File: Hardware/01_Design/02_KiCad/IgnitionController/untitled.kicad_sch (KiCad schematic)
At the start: 26 parts, among them Q4 RSJ250P10, Q5 BC856, Q6 IRF9Z34NSPbF, U3 LM2575-3.3BU, U4 LM2575-5.0BU

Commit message: PMIC HW implementation
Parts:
- added C11: UCL1V101MNL1GS, Capacitor_SMD:CP_Elec_8x11.9, symbol Device:C_Polarized
- added C12: UCL1V331MNL1GS, Capacitor_SMD:CP_Elec_10x12.5, symbol Device:C_Polarized
- added D15: SS14, Diode_SMD:D_SMA, symbol Diode:SS14
- added D16: RED, LED_SMD:LED_0805_2012Metric_Pad1.15x1.40mm_HandSolder, symbol Device:LED
- added L5: L_Iron, Inductor_SMD:L_7.3x7.3_H3.5, symbol Device:L_Iron
- added R23: 470R, Resistor_SMD:R_0805_2012Metric_Pad1.20x1.40mm_HandSolder, symbol Device:R
- added U9: LM2575-5.0BU, Package_TO_SOT_SMD:TO-263-5_TabPin3, symbol Regulator_Switching:LM2575-5.0BU
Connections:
- net GND: now also C11.2, C12.2, D15.2 (A), D16.1 (K), U9.3 (GND), U9.5 (~{ON}/OFF)
- net VCC: now also C11.1, U9.1 (VIN)
- new net: D15.1 (K), L5.1, U9.2 (OUT)
- new net: D16.2 (A), R23.2
- new net VPMIC: C12.1, L5.2, R23.1, U9.4 (FB)
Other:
- note added: "VSEN VMCU and VPMIC power supply"
- note removed: "VSEN and VMCU power supply"

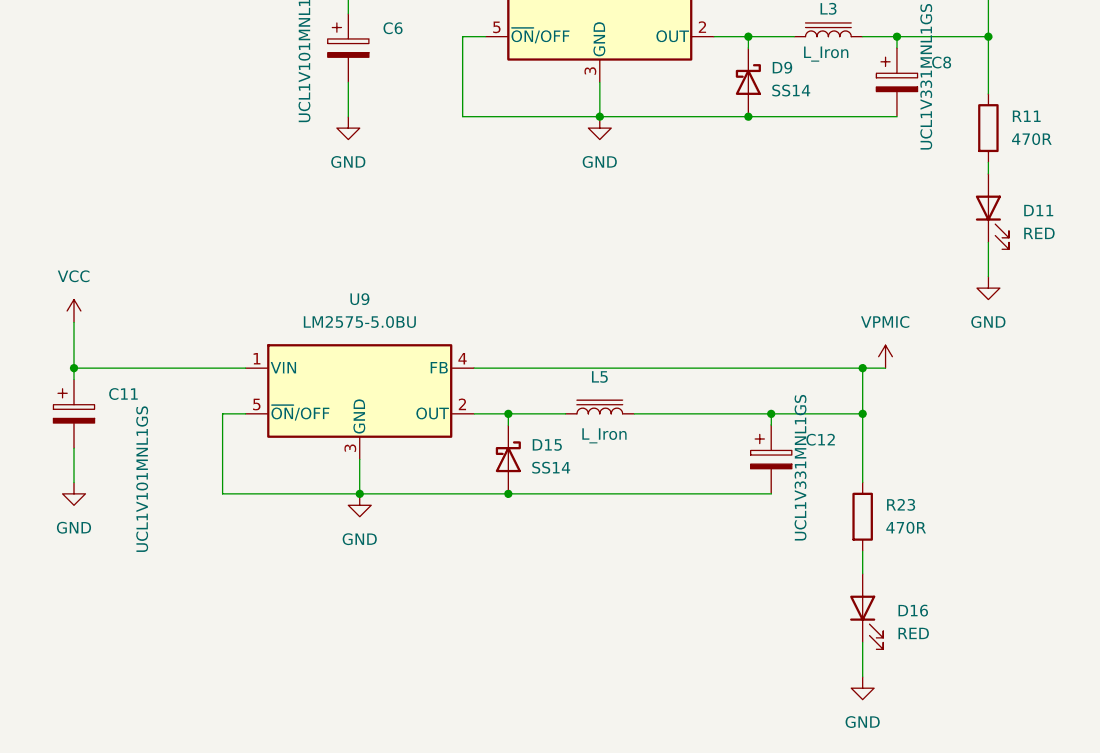
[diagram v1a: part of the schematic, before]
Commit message: Updated sch and footprints
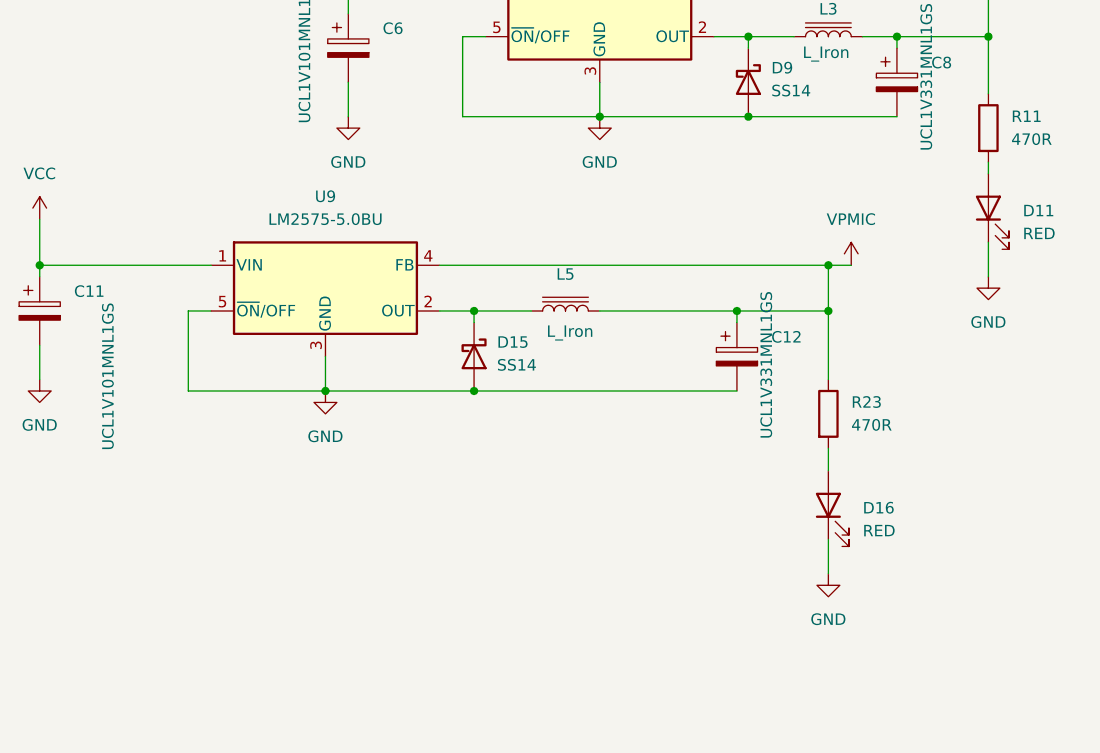
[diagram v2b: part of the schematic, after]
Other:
- moved on the sheet: C11, C12, D15, D16, L5, R23, U9

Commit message: MCU sheet Initial commit
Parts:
- added F1: 2A Fuse, symbol Device:Fuse_Small
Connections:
- net +BATT: now also F1.1; no longer C7.1, Q4.1 (D)
- new net: C7.1, F1.2, Q4.1 (D)
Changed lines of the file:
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@@
 	(wire
 		(pts
+			(xy 57.15 53.34) (xy 45.72 53.34)
+		)
+		(stroke
+			(width 0)
+			(type default)
+		)
+	)
+	(wire
+		(pts
 			(xy 109.22 124.46) (xy 113.03 124.46)
 		)
@@
 	(wire
 		(pts
-			(xy 71.12 53.34) (xy 45.72 53.34)
+			(xy 71.12 53.34) (xy 62.23 53.34)
 		)
 		(stroke
@@
 					(unit 1)
 				)
+			)
+		)
+	)
+	(symbol
+		(lib_id "Device:Fuse_Small")
+		(at 59.69 53.34 0)
+		(unit 1)
+		(exclude_from_sim no)
+		(in_bom yes)
+		(on_board yes)
+		(dnp no)
+		(fields_autoplaced yes)
+		(property "Reference" "F1"
+			(at 59.69 48.26 0)
+			(effects
+				(font
+					(size 1.27 1.27)
+				)
+			)
+		)
+		(property "Value" "2A Fuse"
+			(at 59.69 50.8 0)
+			(effects
+				(font
+					(size 1.27 1.27)
+				)
+			)
+		)
+		(property "Footprint" ""
+			(at 59.69 53.34 0)
+			(effects
+				(font
+					(size 1.27 1.27)
+				)
+				(hide yes)
+			)
+		)
+		(property "Datasheet" "~"
+			(at 59.69 53.34 0)
+			(effects
+				(font
+					(size 1.27 1.27)
+				)
+				(hide yes)
+			)
+		)
+		(property "Description" "Fuse, small symbol"
+			(at 59.69 53.34 0)
+			(effects
+				(font
+					(size 1.27 1.27)
+				)
+				(hide yes)
+			)
+		)
+		(pin "1"
+		)
+		(pin "2"
+		)
+		(instances
+			(project ""
+				(path "/96744ec0-1e7f-4d75-9985-0095978419e2/af36972c-908c-4a23-b0c1-8f51d47880c3"
+					(reference "F1")
+					(unit 1)
+				)

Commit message: Updates to HW Layout
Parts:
- F1: footprint (none) -> Fuse:Fuse_0805_2012Metric_Pad1.15x1.40mm_HandSolder
- renumbered R23 to R57
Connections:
- net at D10.1 (K), R9.2: now also Q5.1 (B)
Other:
- moved on the sheet: D10
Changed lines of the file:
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@@
 	)
 	(junction
-		(at 68.58 119.38)
-		(diameter 0)
-		(color 0 0 0 0)
-	)
-	(junction
 		(at 207.01 125.73)
 		(diameter 0)
@@
 	)
 	(junction
-		(at 45.72 53.34)
+		(at 135.89 48.26)
 		(diameter 0)
 		(color 0 0 0 0)
 	)
 	(junction
-		(at 135.89 48.26)
+		(at 111.76 154.94)
 		(diameter 0)
 		(color 0 0 0 0)
 	)
 	(junction
-		(at 111.76 154.94)
+		(at 68.58 119.38)
 		(diameter 0)
 		(color 0 0 0 0)
@@
 	)
 	(junction
+		(at 119.38 59.69)
+		(diameter 0)
+		(color 0 0 0 0)
+	)
+	(junction
 		(at 121.92 149.86)
 		(diameter 0)
@@
 	(wire
 		(pts
-			(xy 68.58 115.57) (xy 68.58 119.38)
-		)
-		(stroke
-			(width 0)
-			(type default)
-		)
-	)
-	(wire
-		(pts
 			(xy 68.58 121.92) (xy 68.58 119.38)
 		)
@@
 	(wire
 		(pts
-			(xy 87.63 69.85) (xy 87.63 68.58)
+			(xy 119.38 67.31) (xy 119.38 68.58)
 		)
 		(stroke
@@
 	(wire
 		(pts
+			(xy 68.58 115.57) (xy 68.58 119.38)
+		)
+		(stroke
+			(width 0)
+			(type default)
+		)
+	)
+	(wire
+		(pts
 			(xy 101.6 53.34) (xy 101.6 48.26)
 		)
@@
 	(wire
 		(pts
-			(xy 109.22 119.38) (xy 139.7 119.38)
+			(xy 119.38 59.69) (xy 128.27 59.69)
 		)
 		(stroke
@@
 	(wire
 		(pts
-			(xy 119.38 66.04) (xy 119.38 68.58)
+			(xy 109.22 119.38) (xy 139.7 119.38)
 		)
 		(stroke
@@
 	(wire
 		(pts
-			(xy 119.38 59.69) (xy 128.27 59.69)
-		)
-		(stroke
-			(width 0)
-			(type default)
-		)
-	)
-	(wire
-		(pts
 			(xy 190.5 130.81) (xy 190.5 134.62)
 		)
@@
 	(wire
 		(pts
+			(xy 119.38 58.42) (xy 119.38 59.69)
+		)
+		(stroke
+			(width 0)
+			(type default)
+		)
+	)
+	(wire
+		(pts
 			(xy 246.38 140.97) (xy 246.38 143.51)
 		)
@@
 	(symbol
 		(lib_id "Device:D_Zener")
-		(at 119.38 62.23 270)
+		(at 119.38 63.5 270)
 		(unit 1)
 		(exclude_from_sim no)
@@
 		(fields_autoplaced yes)
 		(property "Reference" "D10"
-			(at 121.92 60.9599 90)
+			(at 121.92 62.2299 90)
 			(effects
 				(font
@@
 		)
 		(property "Value" "KDZV18B"
-			(at 121.92 63.4999 90)
+			(at 121.92 64.7699 90)
 			(effects
 				(font
@@
 		)
 		(property "Footprint" "Diode_SMD:D_SOD-123"
-			(at 119.38 62.23 0)
+			(at 119.38 63.5 0)
 			(effects
 				(font
@@
 		)
 		(property "Datasheet" "~"
-			(at 119.38 62.23 0)
+			(at 119.38 63.5 0)
 			(effects
 				(font
@@
 		)
 		(property "Description" "Zener diode"
-			(at 119.38 62.23 0)
+			(at 119.38 63.5 0)
 			(effects
 				(font
@@
 	(symbol
 		(lib_id "power:+BATT")
-		(at 45.72 53.34 0)
+		(at 45.72 52.07 0)
 		(unit 1)
 		(exclude_from_sim no)
@@
 		(fields_autoplaced yes)
 		(property "Reference" "#PWR014"
-			(at 45.72 57.15 0)
+			(at 45.72 55.88 0)
 			(effects
 				(font
@@
 		)
 		(property "Value" "+BATT"
-			(at 45.72 48.26 0)
+			(at 45.72 46.99 0)
 			(effects
 				(font
@@
 		)
 		(property "Footprint" ""
-			(at 45.72 53.34 0)
+			(at 45.72 52.07 0)
 			(effects
 				(font
@@
 		)
 		(property "Datasheet" ""
-			(at 45.72 53.34 0)
+			(at 45.72 52.07 0)
 			(effects
 				(font
@@
 		)
 		(property "Description" "Power symbol creates a global label with name \"+BATT\""
-			(at 45.72 53.34 0)
+			(at 45.72 52.07 0)
 			(effects
 				(font
@@
 			)
 		)
-		(property "Footprint" ""
+		(property "Footprint" "Fuse:Fuse_0805_2012Metric_Pad1.15x1.40mm_HandSolder"
 			(at 59.69 53.34 0)
 			(effects
@@
 		(dnp no)
 		(fields_autoplaced yes)
-		(property "Reference" "R23"
+		(property "Reference" "R57"
 			(at 124.46 165.0999 0)
 			(effects
@@
 			(project "IgnitionController"
 				(path "/96744ec0-1e7f-4d75-9985-0095978419e2/af36972c-908c-4a23-b0c1-8f51d47880c3"
-					(reference "R23")
+					(reference "R57")
 					(unit 1)
 				)
